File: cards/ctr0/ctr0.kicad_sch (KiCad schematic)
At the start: 105 parts, among them J1 BUS, J2 OUT, J3 LINK, Q1 2N7000, Q10 2N7000, Q11 2N7000, Q12 2N7000, Q13 2N7000, Q14 2N7000, Q15 2N7000, Q16 2N7000, Q17 2N7000, Q18 2N7000, Q19 2N7000, Q2 2N7000, Q20 2N7000, Q21 2N7000, Q22 2N7000, Q23 2N7000, Q24 2N7000, Q25 2N7000, Q26 2N7000, Q27 2N7000, Q28 2N7000, Q29 2N7000, Q3 2N7000, Q30 2N7000, Q31 2N7000, Q32 2N7000, Q33 2N7000, Q34 2N7000, Q35 2N7000, Q36 2N7000, Q37 2N7000, Q38 2N7000, Q39 2N7000, Q4 2N7000, Q40 2N7000, Q41 2N7000, Q42 2N7000, Q43 2N7000, Q44 2N7000, Q45 2N7000, Q46 2N7000, Q47 2N7000, Q48 2N7000, Q49 2N7000, Q5 2N7000, Q50 2N7000, Q51 2N7000, Q52 2N7000, Q53 2N7000, Q54 2N7000, Q55 2N7000, Q56 2N7000, Q57 2N7000, Q58 2N7000, Q59 2N7000, Q6 2N7000, Q60 2N7000, Q61 2N7000, Q62 2N7000, Q7 2N7000, Q8 2N7000, Q9 2N7000

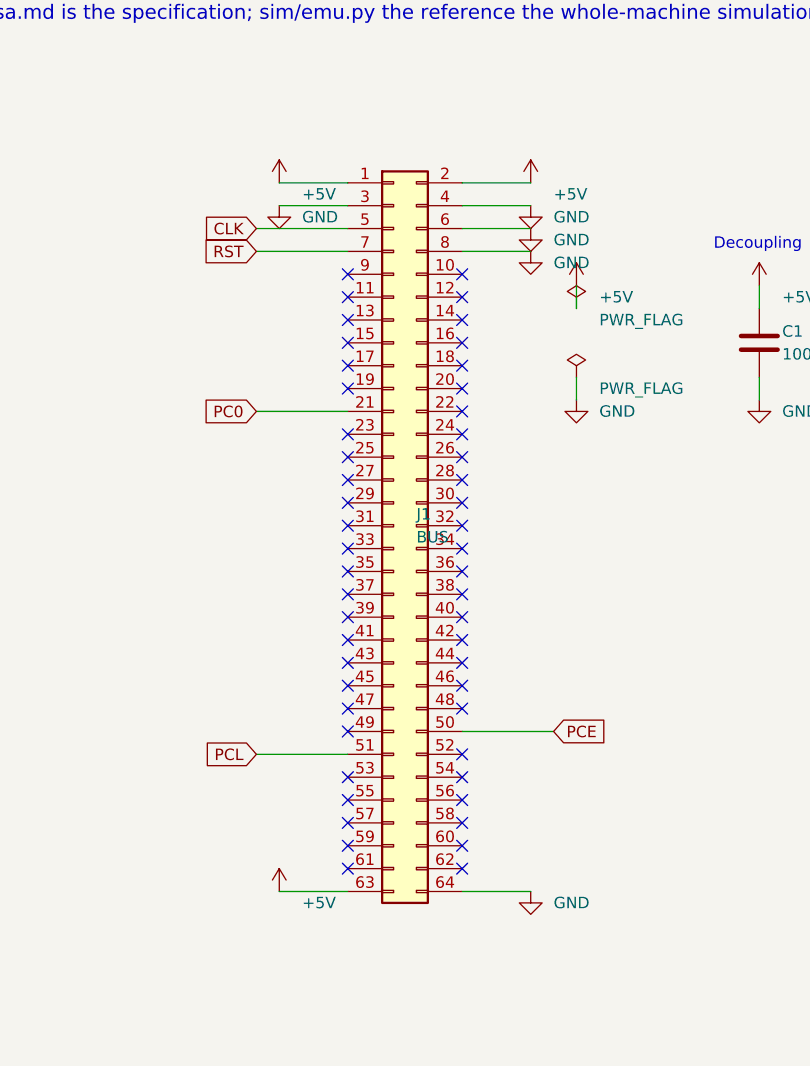
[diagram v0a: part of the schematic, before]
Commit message: The bus headers go on the back of all 26 boards, no track moved; the silkscreen refitted (D059, D062)
An IDC socket lies across its ribbon, so the ribbon could never run along a
row of cards as drawn. It runs behind them, and the 64-pin headers are
soldered on the back. This commit is that move, made in place on the routed
boards: no board was routed again.

How the header sits (D062): in the holes it had, turned over top to bottom,
notch toward the top edge. A pin of the odd row is then in the hole its even
neighbour had, so the two signals of every pair of pins change places: CLK
is pin 6, RST pin 8, +5V pins 1, 2 and 64. bus.py keeps both tables: PINS,
what the header's pins carry, and HOLES, what the copper was routed to.

The proof, on all 26 boards against 992a90f (sim/board_diff.py):
  netlist the same, element for element; every track, every via and every
  hole the same; each copper and mask layer differs by two pad shapes per
  header (pin 1's square went to the hole beside it, both on +5V) and the
  ground pour's outline round those two pads, nowhere else by more than a
  tenth of a micrometre.
sim/rebuild_check.py runs every builder into a scratch directory: each
writes the plan and the netlist that are committed, so a rebuild gives
this board. order_check.py --machine holds every pad of the 27 headers to
bus.py and requires them on the back.

What the move costs: on the ribbon RST had a ground conductor on both
sides; now one neighbour is BUS1#. tb_rst_neighbour.py puts the two lines
on the bench with every gate the routed boards hang on them: RST rises
0.28 to 0.43 V when BUS1# is released, against a lowest threshold of 0.8 V
(sim/results/rst_neighbour.md). The machine deck's crosstalk option now
couples the pins that are neighbours on the ribbon; the crosstalk stage of
the machine gate has to be run again on that order.

Silkscreen (pcb.fit_silk): every label to 1.0 mm where it has room, off
pads, vias, outlines and other labels, out from under the pa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
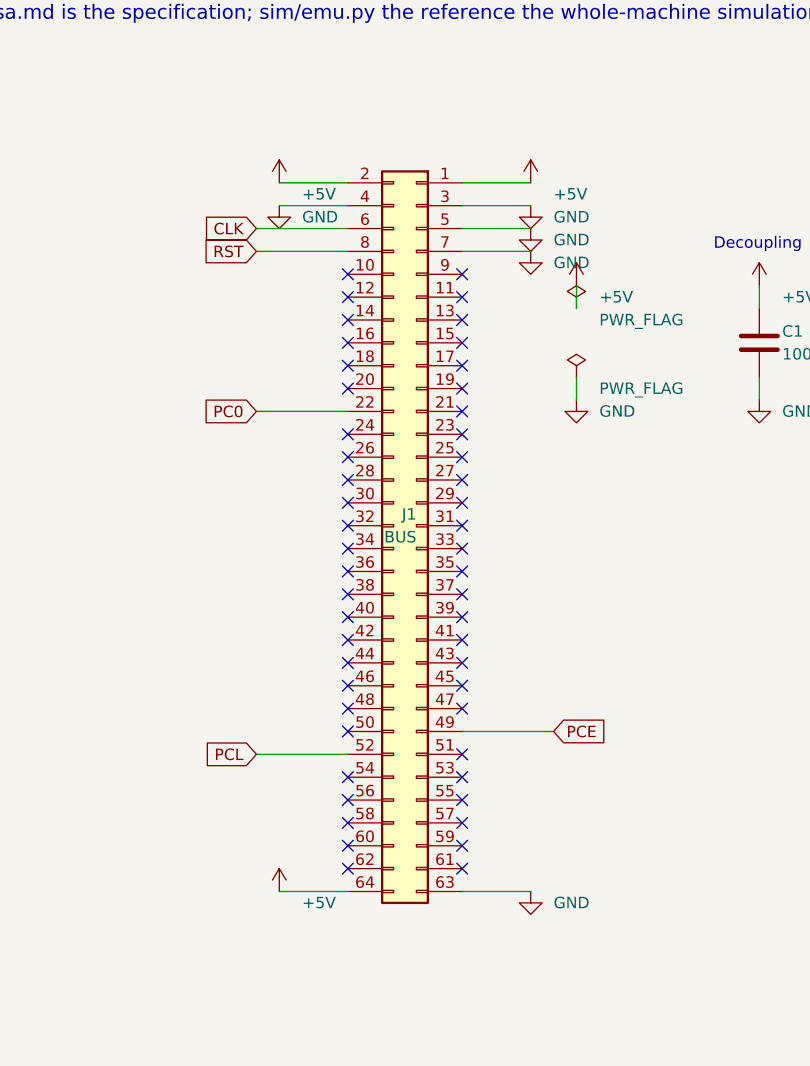
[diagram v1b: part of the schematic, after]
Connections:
- net +5V: now also J1.64 (Pin_64); no longer J1.63 (Pin_63)
- net CLK: now also J1.6 (Pin_6); no longer J1.5 (Pin_5)
- net GND: now also J1.5 (Pin_5), J1.63 (Pin_63), J1.7 (Pin_7); no longer J1.6 (Pin_6), J1.64 (Pin_64), J1.8 (Pin_8)
- net PC0: now also J1.22 (Pin_22); no longer J1.21 (Pin_21)
- net PCE: now also J1.49 (Pin_49); no longer J1.50 (Pin_50)
- net PCL: now also J1.52 (Pin_52); no longer J1.51 (Pin_51)
- net RST: now also J1.8 (Pin_8); no longer J1.7 (Pin_7)
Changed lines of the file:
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@@
 	(symbol
 		(lib_id "Connector_Generic:Conn_02x32_Odd_Even")
-		(at 76.2 101.6 0)
+		(at 78.74 101.6 0)
+		(mirror y)
 		(unit 1)
 		(body_style 1)
